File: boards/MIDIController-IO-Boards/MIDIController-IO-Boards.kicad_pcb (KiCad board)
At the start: 2 copper layers, 150 x 100 mm, 40 parts, among them J1 KeyboardCtrl, J10 I2C, J11 I2CAddr, J12 IO_Boards, J2 TechnicsCtrl, J3 StopLeftCtrl, J4 StopRightCtrl, J5 TCA9548A 1, J6 PanelCtrl, J7 ToeStudCtrl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

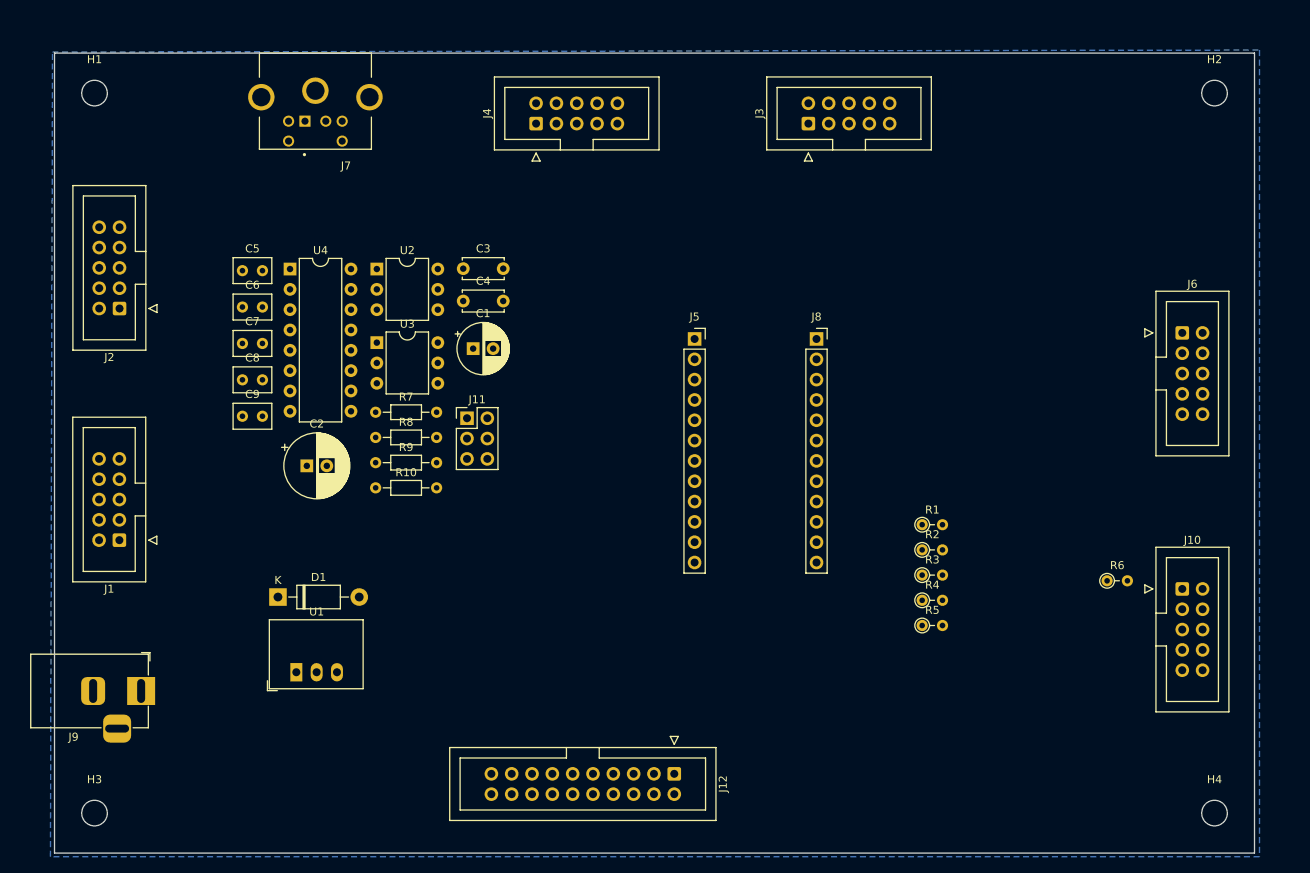
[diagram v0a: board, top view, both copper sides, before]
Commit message: Finished IO-Board PCB, switched RX/TX of board connectors for better routing
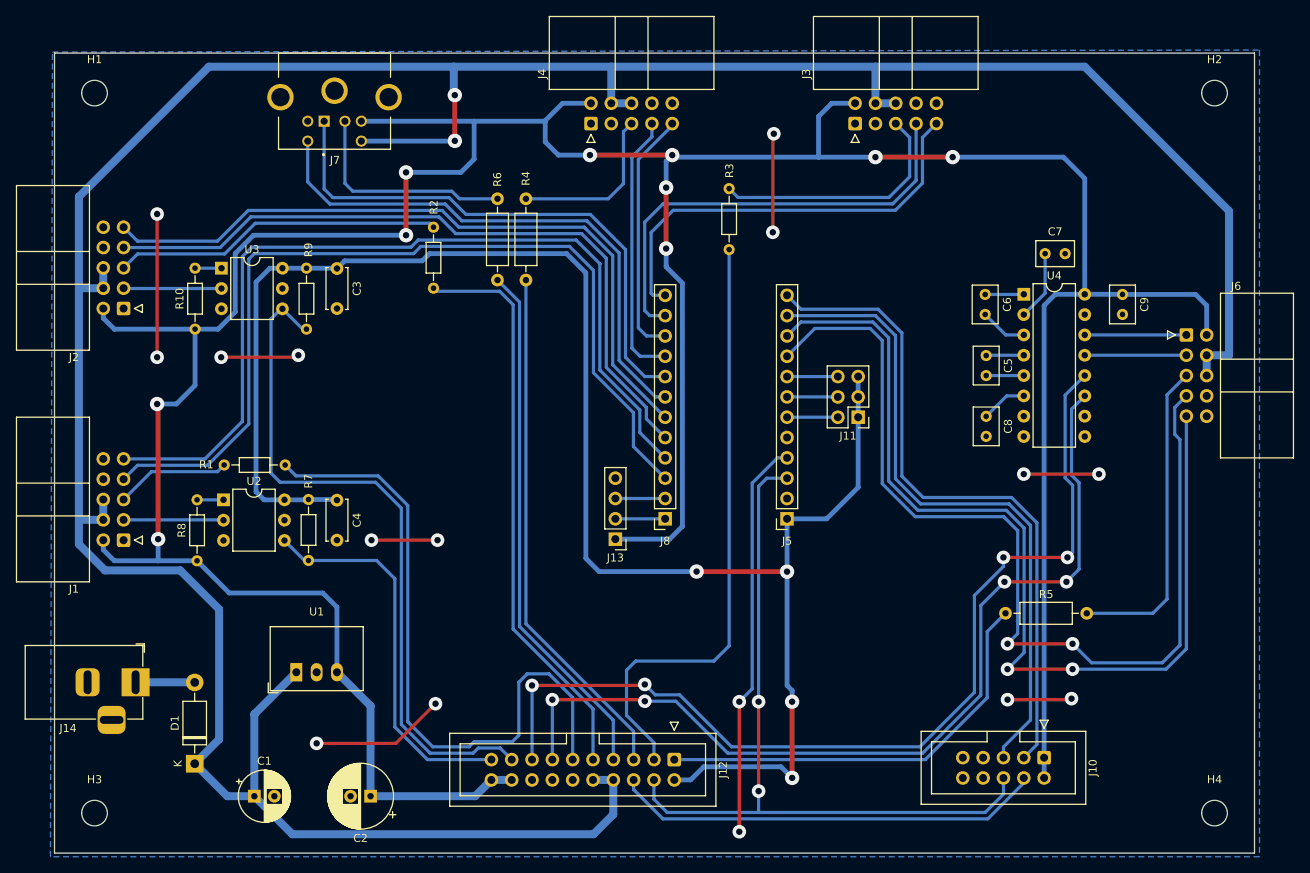
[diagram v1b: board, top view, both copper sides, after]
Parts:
- removed J9: Barrel_Jack_MountingPin, Connector_BarrelJack:BarrelJack_Horizontal
- added J13: I2C2, Connector_PinHeader_2.54mm:PinHeader_1x04_P2.54mm_Vertical, F.Cu at (138.2, 101.2)
- added J14: DC12V, Connector_BarrelJack:BarrelJack_Horizontal, F.Cu at (78.2, 119.1)
- J1, J2, J3, J4, J6: footprint Connector_IDC:IDC-Header_2x05_P2.54mm_Vertical -> Connector_IDC:IDC-Header_2x05_P2.54mm_Horizontal
- R1, R2, R3: footprint Resistor_THT:R_Axial_DIN0204_L3.6mm_D1.6mm_P2.54mm_Vertical -> Resistor_THT:R_Axial_DIN0204_L3.6mm_D1.6mm_P7.62mm_Horizontal
- R4, R5, R6: footprint Resistor_THT:R_Axial_DIN0204_L3.6mm_D1.6mm_P2.54mm_Vertical -> Resistor_THT:R_Axial_DIN0207_L6.3mm_D2.5mm_P10.16mm_Horizontal
- moved C9 111.1 mm to (201.6, 70.6), turned to -90 degrees
- moved C7 101.0 mm to (191.9, 65.5)
- moved C5 93.6 mm to (184.5, 78.3), turned to -90 degrees
- moved C8 93.1 mm to (184.5, 85.9), turned to -90 degrees
- moved C6 92.9 mm to (184.4, 70.6), turned to -90 degrees
- moved U4 91.8 mm to (189.2, 70.6)
- moved R6 85.0 mm to (123.4, 68.8), turned to 90 degrees
- moved R1 80.0 mm to (96.9, 91.9), turned to 180 degrees
- moved R2 69.3 mm to (115.4, 69.8), turned to 90 degrees
- moved R4 63.7 mm to (127.0, 68.8), turned to 90 degrees
- moved C1 62.3 mm to (93.1, 133.3)
- moved J11 48.9 mm to (168.5, 86.0), turned to 180 degrees
- moved R3 47.3 mm to (152.4, 65.0), turned to 90 degrees
- moved C2 42.1 mm to (107.6, 133.3), turned to 180 degrees
- moved U2 34.6 mm to (89.2, 96.3)
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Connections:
- net SCL3 renamed /SCL_StopLeft
- net SCL4 renamed /SCL_StopRight
- net SDA3 renamed /SDA_StopLeft
- net SDA4 renamed /SDA_StopRight
- J1 pad 1: /MIDI_IN_Kbd -> unconnected-(J1-Pin_1-Pad1)
- J1 pad 3: unconnected-(J1-Pin_3-Pad3) -> /MIDI_IN_Kbd
- J1 pad 7: SCL1 -> /SCL_Kbd
- J1 pad 9: SDA1 -> /SDA_Kbd
- J10 pad 1: /SCL -> +5V
- J10 pad 2: SCL8 -> +5V
- J10 pad 3: /SDA -> /SCL_I2C1
- J10 pad 4: SDA8 -> /SCL
- J10 pad 5: +5V -> /SDA_I2C1
- J10 pad 6: +5V -> /SDA
- J11 pad 1: +5V -> +3.3V
- J11 pad 3: +5V -> +3.3V
- J11 pad 5: +5V -> +3.3V
- J12 pad 1: /IntKeyboard -> /IntPanel
- J12 pad 10: /SDA -> +12V
- J12 pad 11: /IntToeStud -> /IntKeyboard
- J12 pad 12: /SCL -> GND
- J12 pad 14: +3.3V -> GND
- J12 pad 17: /RXD_Kbd -> /RXD_Technics
- J12 pad 18: GND -> +5V
- J12 pad 19: /RXD_Technics -> /RXD_Kbd
- J12 pad 2: +12V -> +3.3V
- J12 pad 20: GND -> +5V
- J12 pad 3: /IntTechnics -> /IntStopLeft
- J12 pad 4: +12V -> /SDA
- J12 pad 5: /IntStopLeft -> /IntStopRight
- J12 pad 6: +5V -> /SCL
- J12 pad 7: /IntStopRight -> /IntToeStud
- J12 pad 8: +5V -> +12V
- J12 pad 9: /IntPanel -> /IntTechnics
- J2 pad 1: /MIDI_IN_Technics -> unconnected-(J2-Pin_1-Pad1)
- J2 pad 3: unconnected-(J2-Pin_3-Pad3) -> /MIDI_IN_Technics
- J2 pad 7: SCL2 -> /SCL_Technics
- J2 pad 9: SDA2 -> /SDA_Technics
- J5 pad 10: SCL1 -> /SDA_Panel
- J5 pad 11: SDA2 -> /SDA_I2C1
- J5 pad 12: SCL2 -> /SCL_I2C1
- J5 pad 9: SDA1 -> /SCL_Panel
- J6 pad 1: /RS232_Panel_RXD -> /RS232_Panel_TXD
- J6 pad 3: /RS232_Panel_TXD -> /RS232_Panel_RXD
- J6 pad 7: SCL5 -> /SCL_Panel
- J6 pad 9: SDA5 -> /SDA_Panel
- J7 pad 1: SDA6 -> /SDA_ToeStud
- J7 pad 5: SCL6 -> /SCL_ToeStud
- J8 pad 1: SCL8 -> /SCL_I2C2
- J8 pad 2: SDA8 -> /SDA_I2C2
- J8 pad 3: SCL7 -> /SCL_Kbd
- J8 pad 4: SDA7 -> /SDA_Kbd
- J8 pad 5: SCL6 -> /SCL_Technics
- J8 pad 6: SDA6 -> /SDA_Technics
- J8 pad 7: SCL5 -> /SCL_ToeStud
- J8 pad 8: SDA5 -> /SDA_ToeStud
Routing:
- net +5V: track 0.00 -> 447.4 mm, vias 0 -> 10
- net +12V: track 0.00 -> 394.2 mm, vias 0 -> 2
- net +3.3V: track 0.00 -> 214.8 mm, vias 0 -> 4
- net /SDA_Panel: track 0.00 -> 122.5 mm, vias 0 -> 2
- net /SCL_Panel: track 0.00 -> 121.4 mm, vias 0 -> 2
- net /RXD_Panel: track 0.00 -> 121.2 mm, vias 0 -> 4
- net /TXD_Panel: track 0.00 -> 114.9 mm, vias 0 -> 4
- net /SCL_Kbd: track 0.00 -> 113.8 mm
- net /SDA_Kbd: track 0.00 -> 111.8 mm
- net /SCL: track 0.00 -> 104.9 mm, vias 0 -> 2
- net /SDA: track 0.00 -> 94.5 mm, vias 0 -> 2
- net /SCL_Technics: track 0.00 -> 89.5 mm
- net /SDA_Technics: track 0.00 -> 88.9 mm
- net /RXD_Technics: track 0.00 -> 86.0 mm
- net /SCL_I2C1: track 0.00 -> 83.5 mm
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
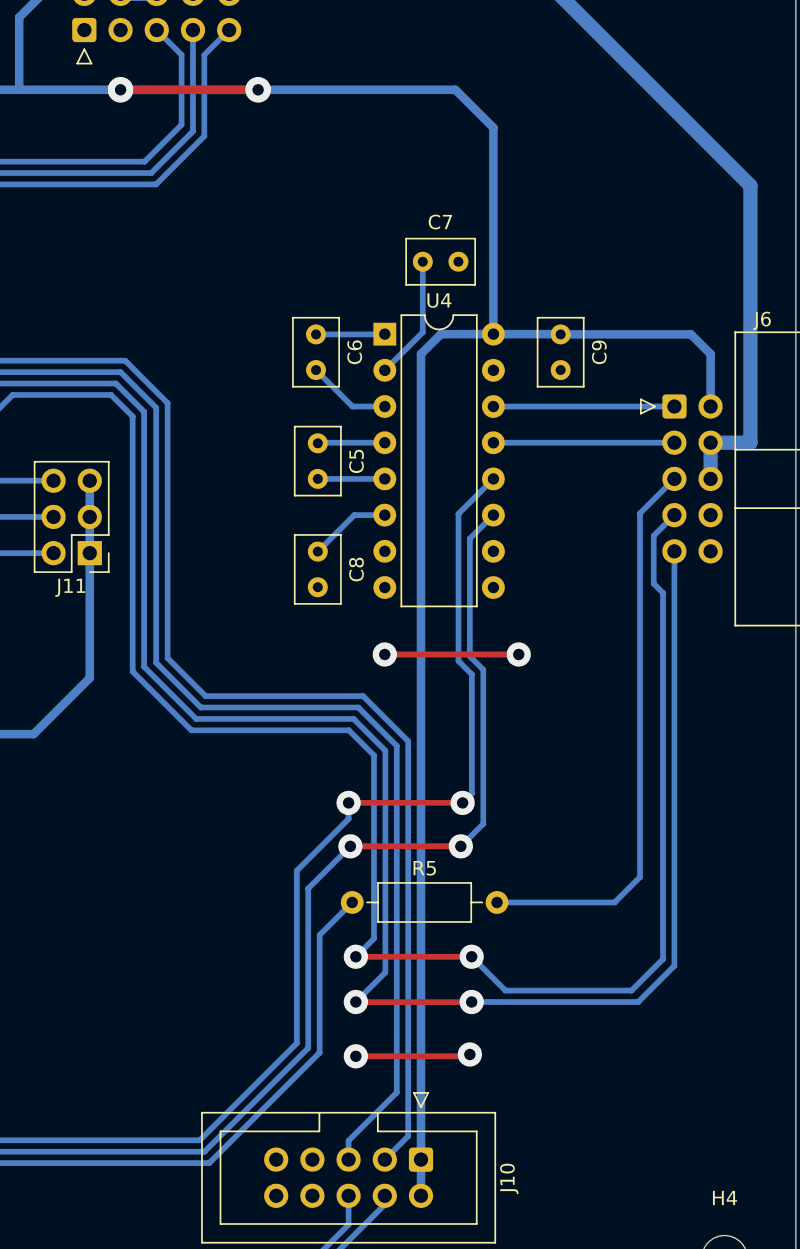
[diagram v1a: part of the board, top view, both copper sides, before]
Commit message: Finished connectors on MIDIController board, fixed 3.3V IO voltage levels
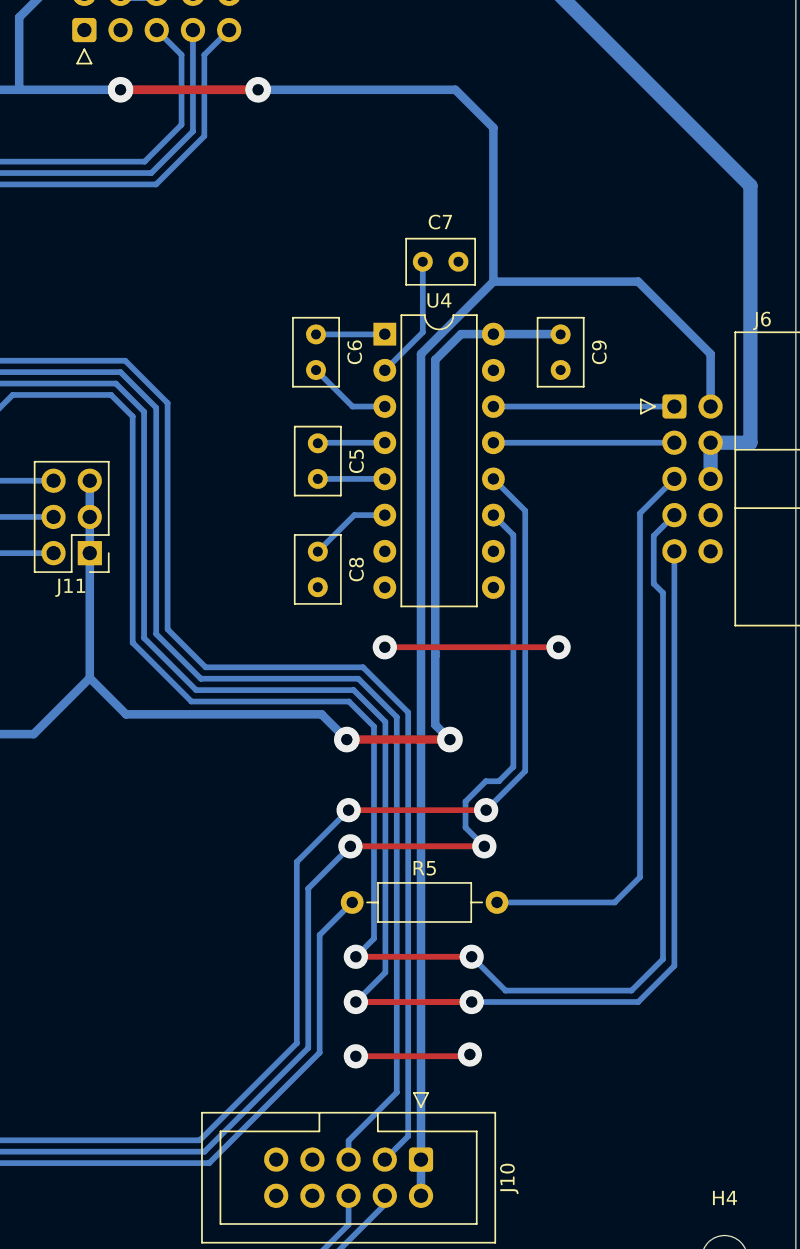
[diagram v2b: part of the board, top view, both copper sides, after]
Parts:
- C5, C6, C7, C8, C9: value 2.2µ -> 0.1uF
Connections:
- C9 pad 1: +5V -> +3.3V
- U4 pad 16: +5V -> +3.3V
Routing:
- net +3.3V: track 214.8 -> 278.5 mm, vias 4 -> 6
- net /RXD_Panel: track 121.2 -> 124.4 mm
- net /TXD_Panel: track 114.9 -> 117.9 mm
- net GND: track 82.7 -> 85.4 mm
- net +5V: track 447.4 -> 446.8 mm

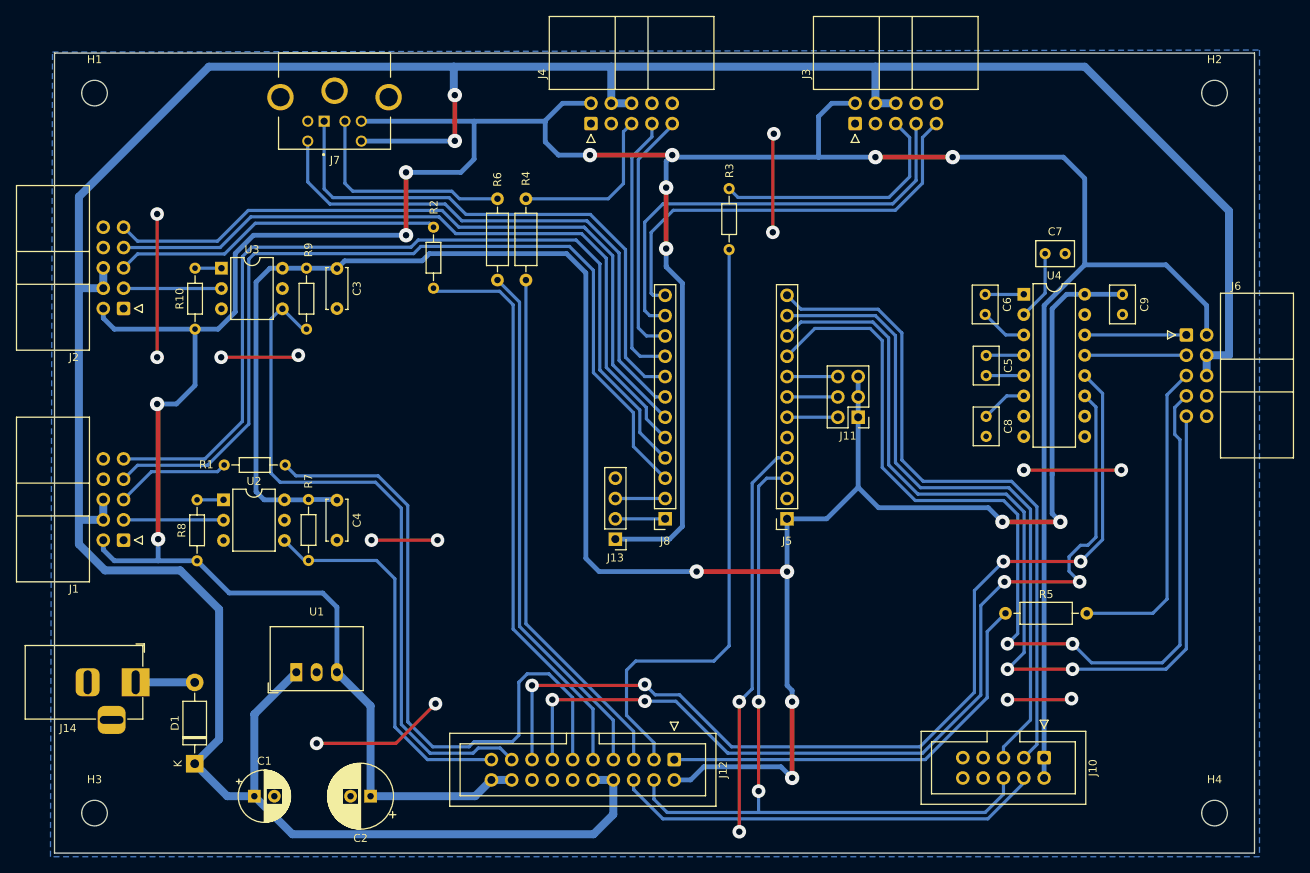
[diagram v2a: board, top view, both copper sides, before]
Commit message: Fixed interrupt line to use open collector, added pullups to I2C lines
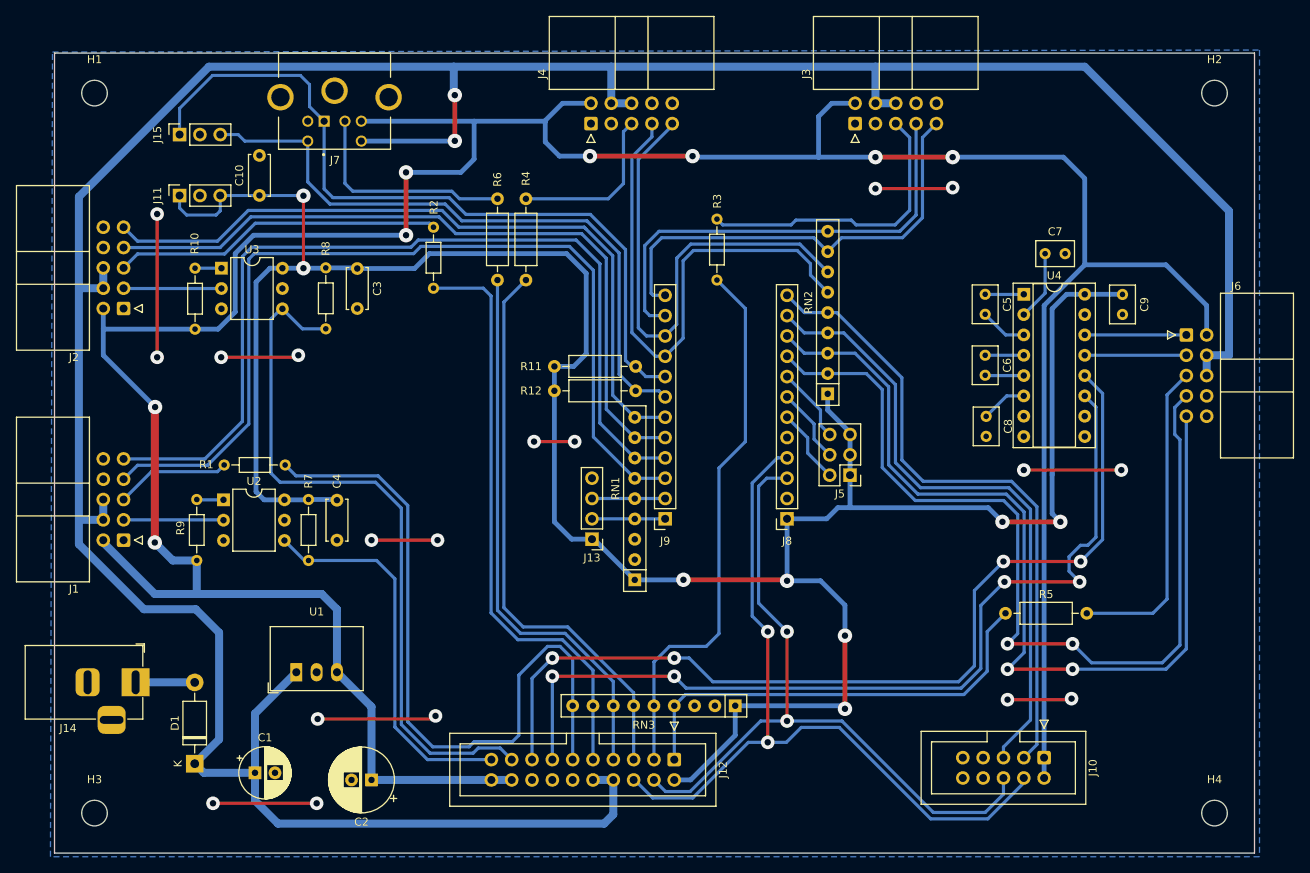
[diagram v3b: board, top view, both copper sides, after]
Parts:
- added C10: 100n, Capacitor_THT:C_Disc_D5.0mm_W2.5mm_P5.00mm, F.Cu at (93.7, 58.3)
- added J15: LTC4311_2, Connector_PinSocket_2.54mm:PinSocket_1x03_P2.54mm_Vertical, F.Cu at (83.7, 50.6)
- added J9: TCA9548A 2, Connector_PinSocket_2.54mm:PinSocket_1x12_P2.54mm_Vertical, F.Cu at (144.4, 98.7)
- added R11: 10k, Resistor_THT:R_Axial_DIN0207_L6.3mm_D2.5mm_P10.16mm_Horizontal, F.Cu at (140.7, 79.6)
- added R12: 10k, Resistor_THT:R_Axial_DIN0207_L6.3mm_D2.5mm_P10.16mm_Horizontal, F.Cu at (140.7, 82.7)
- added RN1: 1.5k, Resistor_THT:R_Array_SIP9, F.Cu at (140.6, 106.3)
- added RN2: 1.5k, Resistor_THT:R_Array_SIP9, F.Cu at (164.7, 83.1)
- added RN3: 1.5k, Resistor_THT:R_Array_SIP9, F.Cu at (153.2, 122.0)
- J11: value I2CAddr -> LTC4311_1; footprint Connector_PinHeader_2.54mm:PinHeader_2x03_P2.54mm_Vertical -> Connector_PinSocket_2.54mm:PinSocket_1x03_P2.54mm_Vertical
- J5: value TCA9548A 1 -> I2CAddr; footprint Connector_PinSocket_2.54mm:PinSocket_1x12_P2.54mm_Vertical -> Connector_PinHeader_2.54mm:PinHeader_2x03_P2.54mm_Vertical
- J8: value TCA9548A 2 -> TCA9548A 1
- R8: value 220 -> 10k
- R9: value 10k -> 220
- U4: footprint Package_DIP:DIP-16_W7.62mm -> Package_DIP:DIP-16_W7.62mm_Socket
- moved J11 89.2 mm to (83.7, 58.3), turned to 90 degrees
- moved R8 40.0 mm to (102.0, 67.3), turned to -90 degrees
- moved R9 39.0 mm to (85.9, 103.9), turned to 90 degrees
- moved J8 15.2 mm to (159.6, 98.7)
- moved J5 9.58 mm to (167.5, 93.2)
- moved C5 7.66 mm to (184.4, 70.6)
- moved C6 7.60 mm to (184.4, 78.2)
- moved R3 4.10 mm to (150.9, 68.8)
- moved C1 2.92 mm to (93.1, 130.4)
- moved J13 2.92 mm to (135.3, 101.2)
- moved C3 2.54 mm to (105.9, 67.4)
- moved C2 2.04 mm to (107.7, 131.3)
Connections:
- net /MIDI_IN_Kbd renamed /Connectors/MIDI_IN_Kbd
- net /MIDI_IN_Technics renamed /Connectors/MIDI_IN_Technics
- net /RS232_Panel_RXD renamed /Connectors/RS232_Panel_RXD
- net /RS232_Panel_TXD renamed /Connectors/RS232_Panel_TXD
- C5 pad 1: Net-(U4-C2+) -> Net-(U4-C1+)
- C5 pad 2: Net-(U4-C2-) -> Net-(U4-C1-)
- C6 pad 1: Net-(U4-C1+) -> Net-(U4-C2+)
- C6 pad 2: Net-(U4-C1-) -> Net-(U4-C2-)
- J11 pad 2: Net-(J11-Pin_2) -> GND
- J13 pad 1: +5V -> +3.3V
- J5 pad 2: GND -> Net-(J5-Pin_2)
- J5 pad 3: /SDA -> +3.3V
- J5 pad 4: /SCL -> Net-(J5-Pin_4)
- J5 pad 5: /RST -> +3.3V
- J5 pad 6: Net-(J11-Pin_2) -> Net-(J5-Pin_6)
- J8 pad 1: /SCL_I2C2 -> +3.3V
- J8 pad 10: /SDA_StopRight -> /SDA_Panel
- J8 pad 11: /SCL_StopLeft -> /SDA_I2C1
- J8 pad 12: /SDA_StopLeft -> /SCL_I2C1
- J8 pad 2: /SDA_I2C2 -> GND
- J8 pad 3: /SCL_Kbd -> /SDA
- J8 pad 4: /SDA_Kbd -> /SCL
- J8 pad 5: /SCL_Technics -> /RST
- J8 pad 6: /SDA_Technics -> Net-(J5-Pin_2)
- J8 pad 7: /SCL_ToeStud -> Net-(J5-Pin_4)
- J8 pad 8: /SDA_ToeStud -> Net-(J5-Pin_6)
- J8 pad 9: /SCL_StopRight -> /SCL_Panel
- R8 pad 1: +5V -> +3.3V
- R8 pad 2: Net-(R8-Pad2) -> /RXD_Technics
- R9 pad 1: +3.3V -> +5V
- R9 pad 2: /RXD_Technics -> Net-(R9-Pad2)
- U2 pad 1: Net-(R8-Pad2) -> Net-(R9-Pad2)
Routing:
- net +5V: track 446.8 -> 394.4 mm, vias 10 -> 8
- net +3.3V: track 278.5 -> 318.8 mm, vias 6 -> 8
- net /SCL_StopRight: track 33.7 -> 67.0 mm
- net /SDA_StopRight: track 30.8 -> 62.2 mm
- net /SDA_ToeStud: track 68.7 -> 95.4 mm
- net GND: track 85.4 -> 98.8 mm, vias 14 -> 18
- net /SCL_ToeStud: track 68.8 -> 81.1 mm
- net Net-(J5-Pin_6): track 0.00 -> 9.45 mm
- net Net-(J5-Pin_2): track 0.00 -> 9.45 mm
- net Net-(J5-Pin_4): track 0.00 -> 9.45 mm
- net /IntStopLeft: track 76.2 -> 68.8 mm
- net /RXD_Panel: track 124.4 -> 117.8 mm
- net /SCL_Panel: track 121.4 -> 114.9 mm
- net Net-(J11-Pin_6): track 6.35 -> 0.00 mm
- net Net-(J11-Pin_4): track 6.35 -> 0.00 mm
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
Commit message: Added bypass caps to power supplies, use cheaper MAX232 IC.
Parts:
- removed U4: MAX3232, Package_DIP:DIP-16_W7.62mm_Socket
- added C11: 100n, Capacitor_THT:C_Disc_D5.0mm_W2.5mm_P5.00mm, F.Cu at (91.3, 108.0)
- added C12: 330nF, Capacitor_THT:C_Disc_D5.0mm_W2.5mm_P5.00mm, F.Cu at (100.0, 136.7)
- added U5: ICL3232, Package_DIP:DIP-16_W7.62mm, F.Cu at (189.2, 70.6)
- C5, C6, C7, C8, C9: value 0.1uF -> 0.47uF
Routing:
- net GND: track 98.8 -> 101.8 mm
